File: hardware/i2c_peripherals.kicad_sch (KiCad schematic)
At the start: 8 parts, among them IC1 BMI270, IC2 SHT45-AD1F-R2, J1 Conn_01x04_Pin

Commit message: Small fixes
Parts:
- C2, C3, C4: Field4 Farnell -> (none); Field5 2611911 -> (none); Field6 RM EMK105 B7104KV-F -> (none); Field7 TAIYO YUDEN EUROPE GMBH -> (none); Field8 110091611 -> (none); MPN (none) -> GRM155R71C104KA88D; Manufacturer (none) -> Murata; Mouser (none) -> https://www.mouser.com/ProductDetail/81-GRM155R71C104KA88; Mouser PN (none) -> 81-GRM155R71C104KA88; Part Description 0.1uF 10% 16V Ceramic Capacitor X7R 0402 (1005 Metric) -> (none)
- IC1: MPN (none) -> BMI270; Manufacturer (none) -> Bosch Sensortec; Manufacturer_Name BOSCH -> (none); Manufacturer_Part_Number BMI270 -> (none); Mouser (none) -> https://www.mouser.com/ProductDetail/262-BMI270; Mouser PN (none) -> 262-BMI270; Mouser Part Number 262-BMI270 -> (none); Mouser Price/Stock https://www.mouser.co.uk/ProductDetail/Bosch-Sensortec/BMI2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 -> (none)
- IC2: MPN (none) -> SHT45-AD1F-R2; Manufacturer (none) -> Sensirion; Manufacturer_Name Sensirion -> (none); Manufacturer_Part_Number SHT45-AD1F-R2 -> (none); Mouser (none) -> https://www.mouser.com/ProductDetail/403-SHT45-AD1F-R2; Mouser PN (none) -> 403-SHT45-AD1F-R2; Mouser Part Number 403-SHT45-AD1F-R2 -> (none); Mouser Price/Stock https://www.mouser.co.uk/ProductDetail/Sensirion/SHT45-AD1F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 -> (none)
- J1: MPN (none) -> SM04B-GHS-TB(LF)(SN); Manufacturer (none) -> JST; Mouser (none) -> https://www.mouser.com/ProductDetail/306-SM04BGHSTBLFSN; Mouser PN (none) -> 306-SM04BGHSTBLFSN
- R4, R5: MPN (none) -> RC0402FR-074K7L; Manufacturer (none) -> Yageo; Mouser (none) -> https://www.mouser.com/ProductDetail/603-RC0402FR-074K7L; Mouser PN (none) -> 603-RC0402FR-074K7L

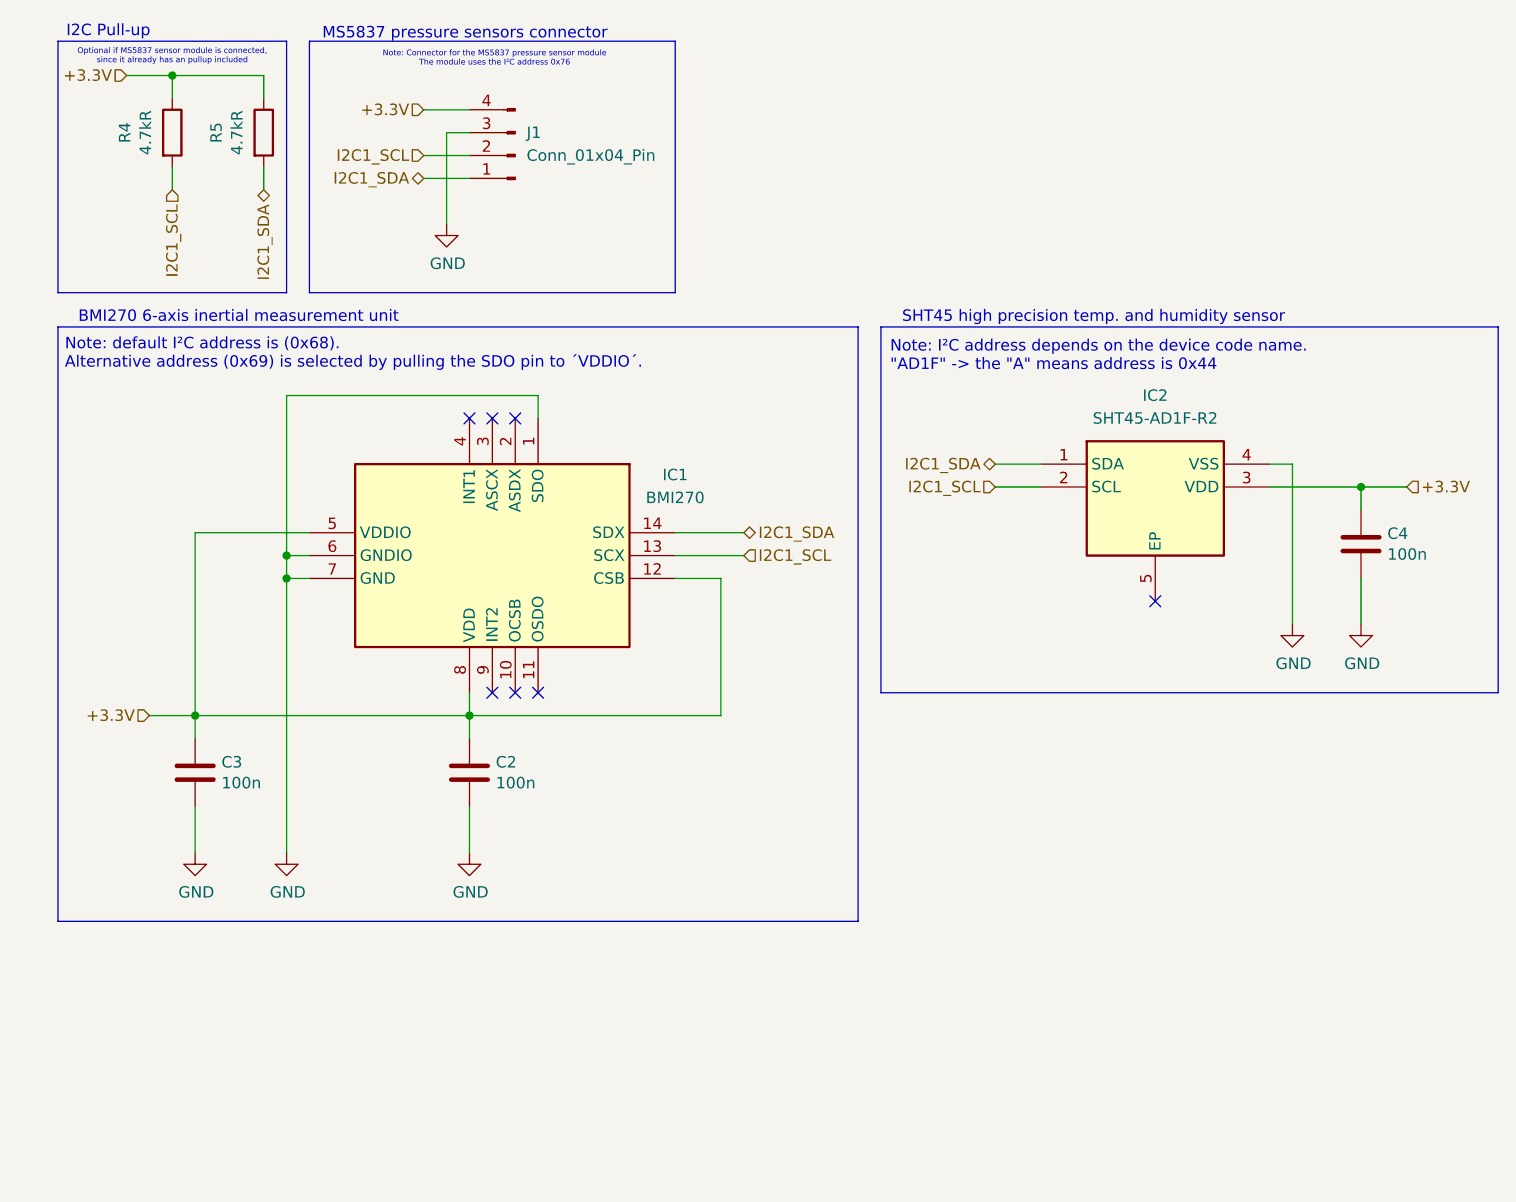
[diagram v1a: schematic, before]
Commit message: Update sensor connection, add 3d files
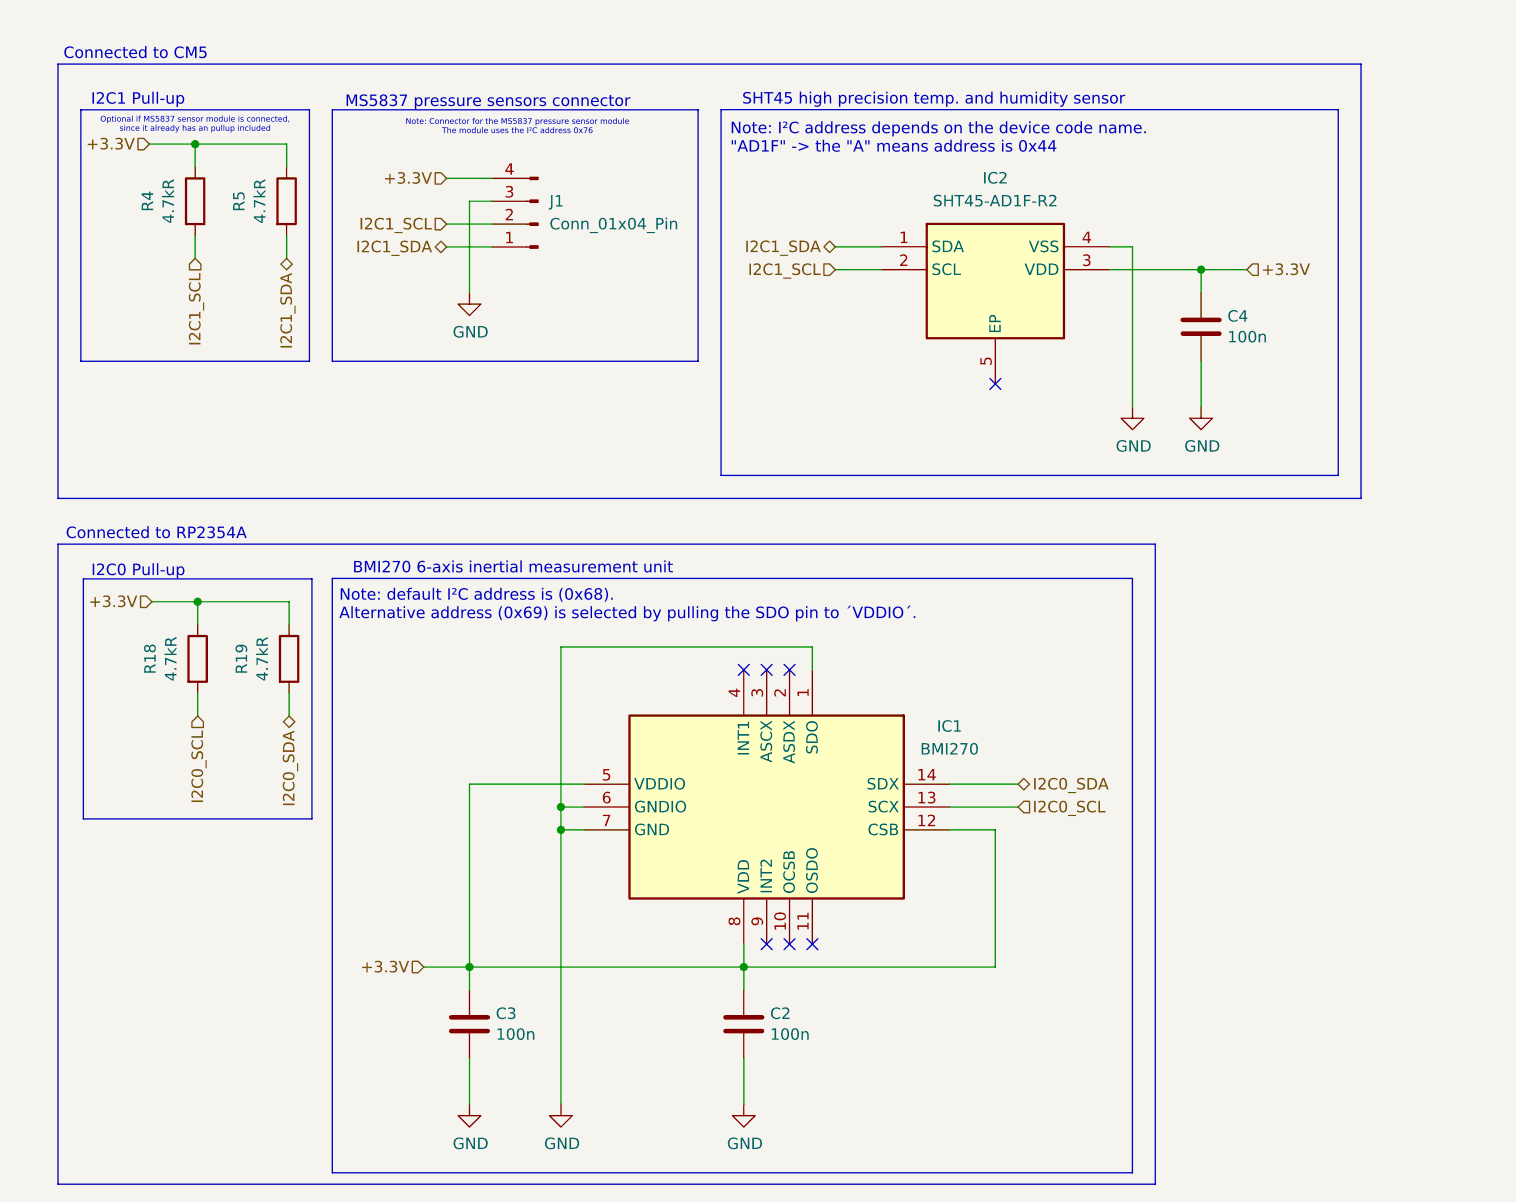
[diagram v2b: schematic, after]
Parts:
- added R18, R19: 4.7kR, Resistor_SMD:R_0402_1005Metric, symbol Device:R
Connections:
- net +3.3V: now also R18.1, R19.1
- net I2C1_SCL: no longer IC1.13 (SCX)
- net I2C1_SDA: no longer IC1.14 (SDX)
- new net I2C0_SCL: IC1.13 (SCX), R18.2
- new net I2C0_SDA: IC1.14 (SDX), R19.2
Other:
- note added: "Connected to CM5"
- note added: "Connected to RP2354A"
- note added: "I2C0 Pull-up"
- note added: "I2C1 Pull-up"
- note removed: "I2C Pull-up"
- moved on the sheet: C2, C3, C4, IC1, IC2, J1, R4, R5
